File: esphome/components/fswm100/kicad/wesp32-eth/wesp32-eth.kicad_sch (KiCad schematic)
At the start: 21 parts, among them J1 Bi-Directional 3.3V-5V Shifte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, J2 ESP32 DEVKITV1 (ESP-WROOM-32), U1 ADS1115IDGS, U2 L7805, U3 TCRT5000, U4 L7805

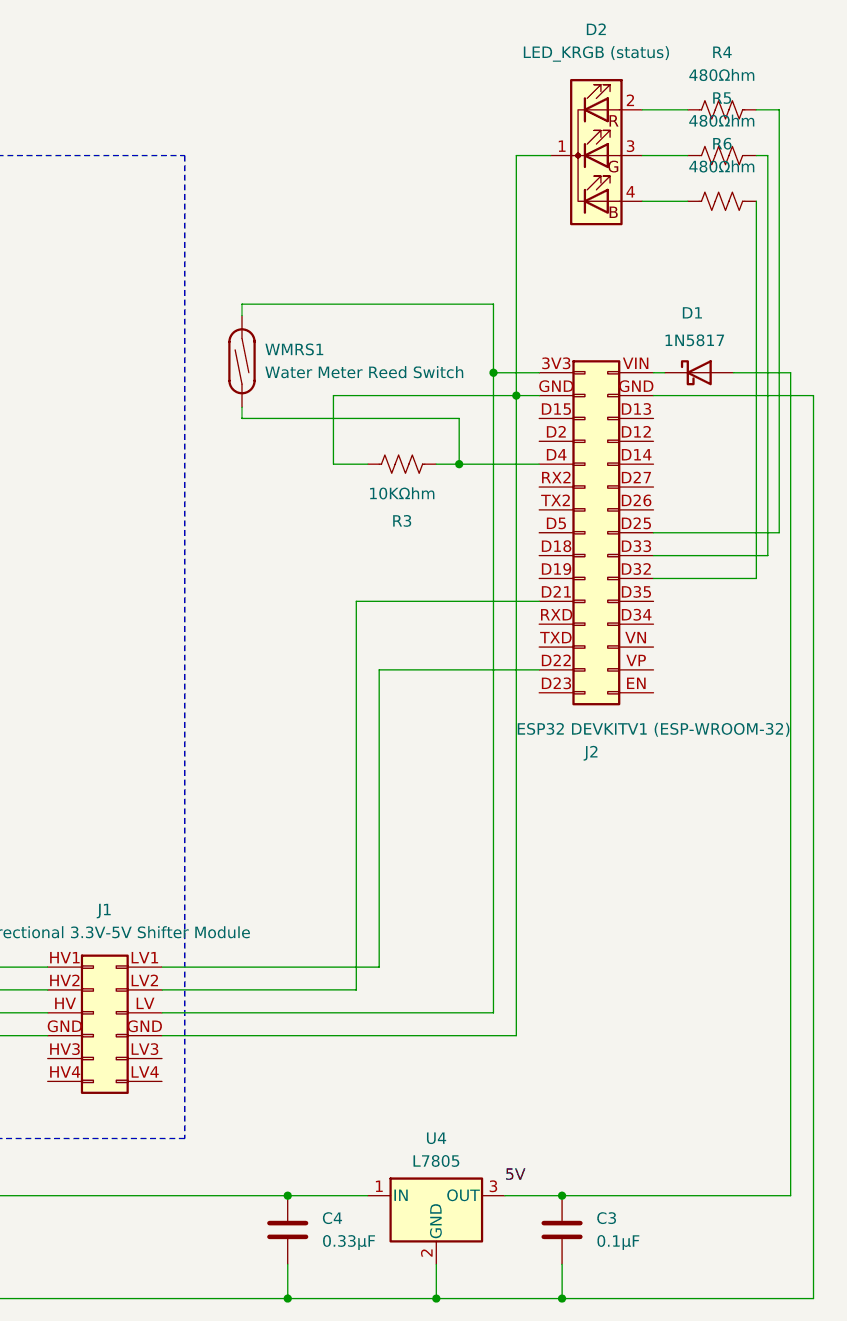
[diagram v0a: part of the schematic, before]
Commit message: fix wesp32 eth circuit
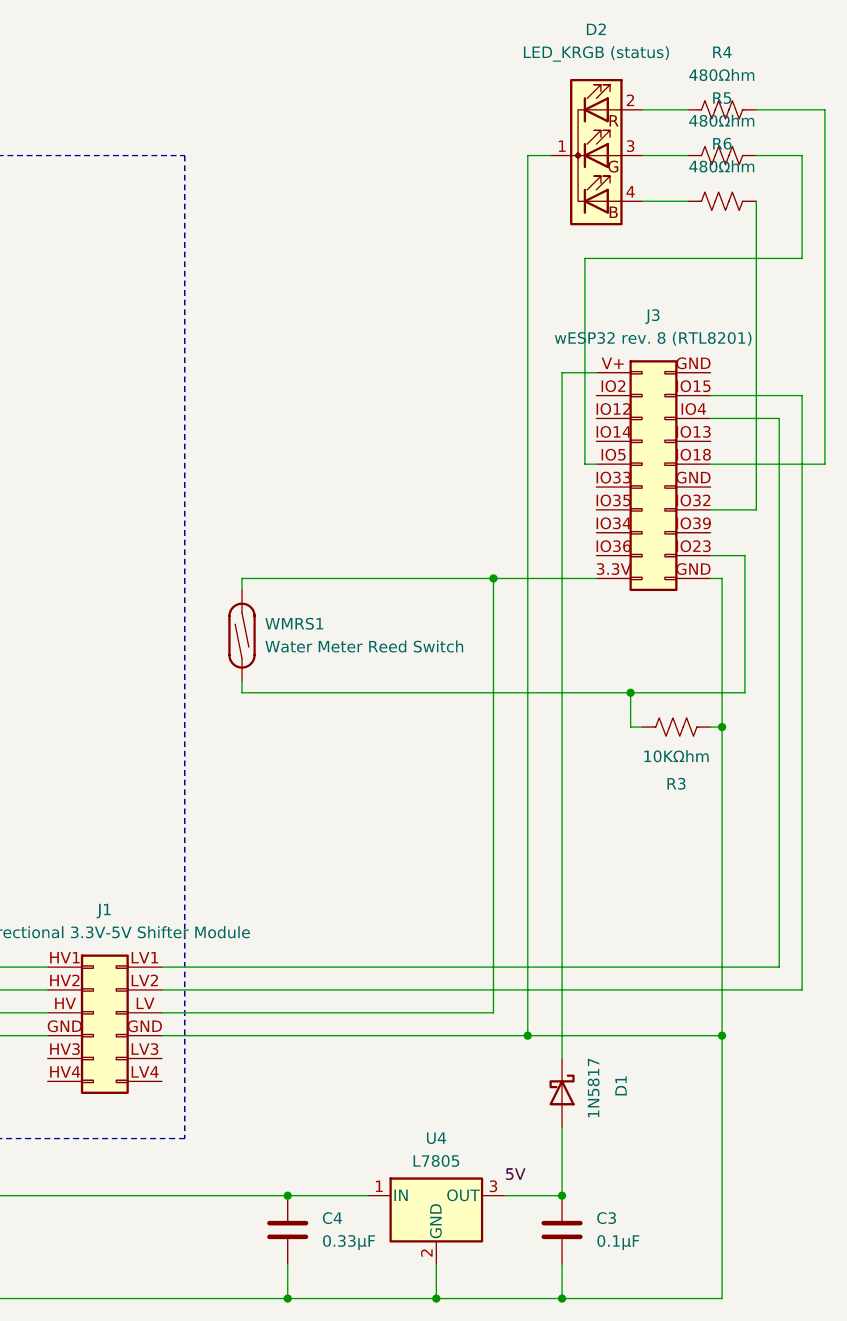
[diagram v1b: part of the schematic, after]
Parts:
- removed J2: ESP32 DEVKITV1 (ESP-WROOM-32), symbol Connector_Generic:Conn_02x15_Top_Bottom
- added J3: wESP32 rev. 8 (RTL8201), symbol Connector:DIN41612_02x10_AB
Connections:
- net D: 2.5mm - 3.5cm: now also D2.1 (K), R3.1, J3.GND (Pin_b10)
- net at WMRS1.1: now also R3.2, J3.IO23 (Pin_b9); no longer R3.1
- net at R6.2: now also J3.IO32 (Pin_b7)
- net at J1.LV (Pin_10), WMRS1.2: now also J3.3.3V (Pin_a10)
- net at J1.LV1 (Pin_12): now also J3.IO4 (Pin_b3)
- net at J1.LV2 (Pin_11): now also J3.IO15 (Pin_b2)
- net at R4.2: now also J3.IO18 (Pin_b5)
- net at R5.2: now also J3.IO5 (Pin_a5)
- net at D1.1 (K): now also J3.V+ (Pin_a1)
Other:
- moved on the sheet: D1, R3, WMRS1
